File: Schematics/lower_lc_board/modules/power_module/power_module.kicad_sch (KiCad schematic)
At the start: 34 parts, among them J1 Stack Male Edge Connector, U1 TVS3300DRV, U10 ID_LM66100DCKR, U2 AMS1117, U3 ID_LM66100DCKR, U4 ID_LM66100DCKR

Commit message: routing work
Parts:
- added C50: 10uF, Capacitor_SMD:C_0603_1608Metric, symbol Device:C
- added C51: 1nF, Capacitor_SMD:C_0402_1005Metric, symbol Device:C
- added C52: 0.1uF, Capacitor_SMD:C_0402_1005Metric, symbol Device:C
- added TP13: 5V-TP, TestPoint:TestPoint_Pad_D1.0mm, symbol Connector:TestPoint
- C47: JLCPCB (none) -> C14663
- C7, C8: JLCPCB (none) -> C96446
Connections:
- net +3V3: now also C50.1, C51.1, C52.1
- net +5V: now also TP13.1
- net GND: now also C50.2, C51.2, C52.2

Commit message: routing work
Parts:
- R1: value 150 -> 220; footprint Resistor_SMD:R_0603_1608Metric -> Resistor_SMD:R_0402_1005Metric; JLCPCB (none) -> C25104
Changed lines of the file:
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@@
 			)
 		)
-		(property "Value" "150"
+		(property "Value" "220"
 			(at 66.04 102.87 90)
 			(effects
@@
 			)
 		)
-		(property "Footprint" "Resistor_SMD:R_0603_1608Metric"
+		(property "Footprint" "Resistor_SMD:R_0402_1005Metric"
 			(at 64.262 102.87 90)
 			(effects
@@
 			(at 66.04 102.87 0)
 			(effects
+				(font
+					(size 1.27 1.27)
+				)
+				(hide yes)
+			)
+		)
+		(property "JLCPCB" "C25104"
+			(at 66.04 102.87 0)
+			(effects

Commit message: routing work
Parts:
- removed C8: 10uF, Capacitor_SMD:C_0603_1608Metric, symbol Device:C
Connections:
- net 3V3_USB is gone; now on net GND: C6.1, TP6.1, U2.2 (VO), U4.1 (VIN)
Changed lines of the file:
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@@
 	)
 	(junction
-		(at 168.91 134.62)
-		(diameter 0)
-		(color 0 0 0 0)
-	)
-	(junction
 		(at 198.12 52.07)
 		(diameter 0)
@@
 	)
 	(junction
+		(at 168.91 134.62)
+		(diameter 0)
+		(color 0 0 0 0)
+	)
+	(junction
 		(at 208.28 62.23)
 		(diameter 0)
@@
 	(wire
 		(pts
+			(xy 168.91 134.62) (xy 190.5 134.62)
+		)
+		(stroke
+			(width 0)
+			(type default)
+		)
+	)
+	(wire
+		(pts
 			(xy 147.32 46.99) (xy 142.24 46.99)
 		)
@@
 	(wire
 		(pts
-			(xy 168.91 134.62) (xy 167.64 134.62)
+			(xy 167.64 134.62) (xy 168.91 134.62)
 		)
 		(stroke
@@
 	(wire
 		(pts
+			(xy 168.91 134.62) (xy 168.91 142.24)
+		)
+		(stroke
+			(width 0)
+			(type default)
+		)
+	)
+	(wire
+		(pts
 			(xy 87.63 133.35) (xy 87.63 134.62)
 		)
@@
 	(wire
 		(pts
-			(xy 168.91 134.62) (xy 190.5 134.62)
-		)
-		(stroke
-			(width 0)
-			(type default)
-		)
-	)
-	(wire
-		(pts
 			(xy 91.44 143.51) (xy 91.44 142.24)
 		)
@@
 		)
 	)
+	(label "3V3_USB"
+		(at 168.91 139.7 0)
+		(fields_autoplaced yes)
+		(effects
+			(font
+				(size 1.27 1.27)
+				(thickness 0.1588)
+			)
+			(justify left bottom)
+		)
+	)
 	(label "3V3_BP"
 		(at 106.68 38.1 180)
@@
 					(unit 1)
 				)
-			)
-		)
-	)
-	(symbol
-		(lib_id "Device:C")
-		(at 168.91 138.43 0)
-		(unit 1)
-		(exclude_from_sim no)
-		(in_bom yes)
-		(on_board yes)
-		(dnp no)
-		(property "Reference" "C8"
-			(at 171.45 137.16 0)
-			(effects
-				(font
-					(size 1.27 1.27)
-				)
-				(justify left)
-			)
-		)
-		(property "Value" "10uF"
-			(at 171.45 139.7 0)
-			(effects
-				(font
-					(size 1.27 1.27)
-				)
-				(justify left)
-			)
-		)
-		(property "Footprint" "Capacitor_SMD:C_0603_1608Metric"
-			(at 169.8752 142.24 0)
-			(effects
-				(font
-					(size 1.27 1.27)
-				)
-				(hide yes)
-			)
-		)
-		(property "Datasheet" "~"
-			(at 168.91 138.43 0)
-			(effects
-				(font
-					(size 1.27 1.27)
-				)
-				(hide yes)
-			)
-		)
-		(property "Description" ""
-			(at 168.91 138.43 0)
-			(effects
-				(font
-					(size 1.27 1.27)
-				)
-				(hide yes)
-			)
-		)
-		(property "LCSC" "C96446"
-			(at 168.91 138.43 0)
-			(effects
-				(font
-					(size 1.27 1.27)
-				)
-				(hide yes)
-			)
-		)
-		(property "JLCPCB" "C96446"
-			(at 168.91 138.43 0)
-			(effects
-				(font
-					(size 1.27 1.27)
-				)
-				(hide yes)
-			)
-		)
-		(pin "1"
-		)
-		(pin "2"
-		)
-		(instances
-			(project "lower_lc_board"
-				(path "/d63798c4-e363-437e-9012-e4aff32e6642/ea1dc739-d1f4-46a0-a090-2a1bf39da427"
-					(reference "C8")
-					(unit 1)
-				)

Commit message: more routing work
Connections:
- net GND: no longer C6.1, TP6.1, U2.2 (VO), U4.1 (VIN)
- new net 3V3_USB: C6.1, TP6.1, U2.2 (VO), U4.1 (VIN)
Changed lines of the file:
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@@
-	)
-	(junction
-		(at 168.91 134.62)
-		(diameter 0)
-		(color 0 0 0 0)
 	)
 	(junction
@@
 	(wire
 		(pts
-			(xy 168.91 134.62) (xy 190.5 134.62)
-		)
-		(stroke
-			(width 0)
-			(type default)
-		)
-	)
-	(wire
-		(pts
 			(xy 147.32 46.99) (xy 142.24 46.99)
 		)
@@
 	(wire
 		(pts
-			(xy 167.64 134.62) (xy 168.91 134.62)
+			(xy 167.64 134.62) (xy 190.5 134.62)
 		)
 		(stroke
@@
 	(wire
 		(pts
-			(xy 168.91 134.62) (xy 168.91 142.24)
-		)
-		(stroke
-			(width 0)
-			(type default)
-		)
-	)
-	(wire
-		(pts
 			(xy 87.63 133.35) (xy 87.63 134.62)
 		)
@@
 		(pts
 			(xy 87.63 134.62) (xy 86.36 134.62)
-		)
-		(stroke
-			(width 0)
-			(type default)
-		)
-	)
-	(wire
-		(pts
-			(xy 160.02 142.24) (xy 168.91 142.24)
 		)
 		(stroke
@@
 		(fields_autoplaced yes)
 		(effects
-			(font
-				(size 1.27 1.27)
-				(thickness 0.1588)
-			)
-			(justify left bottom)
-		)
-	)
-	(label "3V3_USB"
-		(at 168.91 139.7 0)
-		(fields_autoplaced yes)
-		(effects

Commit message: routing work
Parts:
- removed C1: 47uF, Capacitor_SMD:C_1206_3216Metric, symbol Device:C
- removed C47: 0.1uF, Capacitor_SMD:C_0603_1608Metric, symbol Device:C
- removed TP1: 24V_BP, TestPoint:TestPoint_Pad_D1.0mm, symbol Connector:TestPoint
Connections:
- net GND is gone; now on net +3V3: C2.2, C3.2, C4.2, C44.2, C5.1, C50.2, C51.2, C52.2, C6.2, C7.2, D1.1 (K), D2.1 (K), D3.1 (K), D4.1 (K), J1.A12 (GND_B), J1.A3 (GND_A), J1.A6 (GND_A), J1.A9 (GND_B), J1.B10 (GND_B), J1.B11 (GND_B), J1.B12 (GND_B), J1.B15 (GND_C), J1.B16 (GND_C), J1.B17 (GND_C), J1.B18 (GND_C), J1.B4 (GND_A), J1.B5 (GND_A), J1.B6 (GND_A), NT1.2, TP5.1, U1.1 (GND), U1.2 (GND), U1.3 (GND), U1.7 (GND), U10.2 (GND), U10.5 (ST), U2.1 (ADJ), U3.2 (GND), U3.5 (ST), U4.2 (GND), U4.5 (ST)
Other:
- moved on the sheet: TP2

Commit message: analog routing, start 3V3 power routing
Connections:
- net +3V3: no longer C2.2, C3.2, C4.2, C44.2, C5.1, C50.2, C51.2, C52.2, C6.2, C7.2, D1.1 (K), D2.1 (K), D3.1 (K), D4.1 (K), J1.A12 (GND_B), J1.A3 (GND_A), J1.A6 (GND_A), J1.A9 (GND_B), J1.B10 (GND_B), J1.B11 (GND_B), J1.B12 (GND_B), J1.B15 (GND_C), J1.B16 (GND_C), J1.B17 (GND_C), J1.B18 (GND_C), J1.B4 (GND_A), J1.B5 (GND_A), J1.B6 (GND_A), NT1.2, TP5.1, U1.1 (GND), U1.2 (GND), U1.3 (GND), U1.7 (GND), U10.2 (GND), U10.5 (ST), U2.1 (ADJ), U3.2 (GND), U3.5 (ST), U4.2 (GND), U4.5 (ST)
- new net GND: C2.2, C3.2, C4.2, C44.2, C5.1, C50.2, C51.2, C52.2, C6.2, C7.2, D1.1 (K), D2.1 (K), D3.1 (K), D4.1 (K), J1.A12 (GND_B), J1.A3 (GND_A), J1.A6 (GND_A), J1.A9 (GND_B), J1.B10 (GND_B), J1.B11 (GND_B), J1.B12 (GND_B), J1.B15 (GND_C), J1.B16 (GND_C), J1.B17 (GND_C), J1.B18 (GND_C), J1.B4 (GND_A), J1.B5 (GND_A), J1.B6 (GND_A), NT1.2, TP5.1, U1.1 (GND), U1.2 (GND), U1.3 (GND), U1.7 (GND), U10.2 (GND), U10.5 (ST), U2.1 (ADJ), U3.2 (GND), U3.5 (ST), U4.2 (GND), U4.5 (ST)
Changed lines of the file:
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@@
 	)
 	(junction
-		(at 60.96 114.3)
-		(diameter 0)
-		(color 0 0 0 0)
-	)
-	(junction
 		(at 142.24 46.99)
 		(diameter 0)
@@
 		(color 194 0 0 1)
 	)
-	(junction
-		(at 55.88 99.06)
-		(diameter 0)
-		(color 0 0 0 0)
-	)
 	(no_connect
 		(at 95.25 60.96)
@@
 	(wire
 		(pts
-			(xy 60.96 114.3) (xy 66.04 114.3)
-		)
-		(stroke
-			(width 0)
-			(type default)
-		)
-	)
-	(wire
-		(pts
 			(xy 96.52 93.98) (xy 100.33 93.98)
 		)
@@
 	(wire
 		(pts
-			(xy 55.88 99.06) (xy 55.88 114.3)
-		)
-		(stroke
-			(width 0)
-			(type default)
-		)
-	)
-	(wire
-		(pts
 			(xy 190.5 64.77) (xy 189.23 64.77)
 		)
@@
 	(wire
 		(pts
-			(xy 55.88 114.3) (xy 60.96 114.3)
-		)
-		(stroke
-			(width 0)
-			(type default)
-		)
-	)
-	(wire
-		(pts
 			(xy 198.12 62.23) (xy 198.12 72.39)
 		)
@@
 	(symbol
 		(lib_id "power:GND")
-		(at 60.96 114.3 0)
+		(at 66.04 114.3 0)
 		(unit 1)
 		(exclude_from_sim no)
@@
 		(dnp no)
 		(property "Reference" "#PWR03"
-			(at 60.96 120.65 0)
+			(at 66.04 120.65 0)
 			(effects
 				(font
@@
 		)
 		(property "Value" "GND"
-			(at 60.96 118.618 0)
+			(at 66.04 118.618 0)
 			(effects
 				(font
@@
 		)
 		(property "Footprint" ""
-			(at 60.96 114.3 0)
+			(at 66.04 114.3 0)
 			(effects
 				(font
@@
 		)
 		(property "Datasheet" ""
-			(at 60.96 114.3 0)
+			(at 66.04 114.3 0)
 			(effects
 				(font
@@
 		)
 		(property "Description" "Power symbol creates a global label with name \"GND\" , ground"
-			(at 60.96 114.3 0)
+			(at 66.04 114.3 0)
 			(effects
 				(font

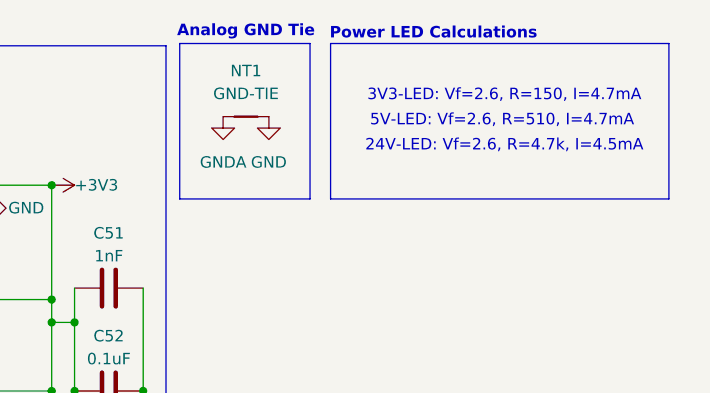
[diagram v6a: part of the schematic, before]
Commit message: remove AGND
simplicity
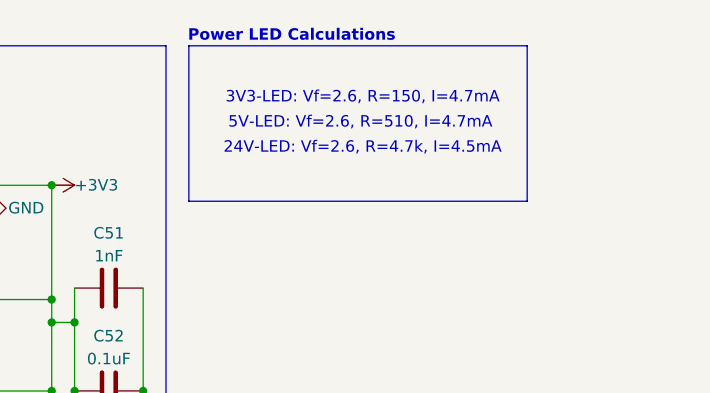
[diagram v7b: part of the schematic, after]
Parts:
- removed NT1: GND-TIE, NetTie:NetTie-2_SMD_Pad0.5mm, symbol Device:NetTie_2
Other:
- note removed: "Analog GND Tie"
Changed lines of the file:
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@@
 	)
 	(rectangle
-		(start 229.108 23.622)
-		(end 266.7 40.894)
+		(start 213.36 23.876)
+		(end 250.952 41.148)
 		(stroke
 			(width 0)
@@
 	)
 	(rectangle
-		(start 212.344 23.622)
-		(end 226.822 40.894)
-		(stroke
-			(width 0)
-			(type default)
-			(color 0 0 0 1)
-		)
-		(fill
-			(type none)
-		)
-	)
-	(rectangle
 		(start 130.302 23.876)
 		(end 210.82 101.6)
@@
 	(text "24V-LED: Vf=2.6, R=4.7k, I=4.5mA"
 		(exclude_from_sim no)
-		(at 248.412 35.052 0)
+		(at 232.664 35.306 0)
 		(effects
 			(font
@@
 	(text "3V3-LED: Vf=2.6, R=150, I=4.7mA"
 		(exclude_from_sim no)
-		(at 248.412 29.464 0)
+		(at 232.664 29.718 0)
 		(effects
 			(font
@@
 		)
 	)
-	(text "Analog GND Tie"
-		(exclude_from_sim no)
-		(at 219.71 22.352 0)
-		(effects
-			(font
-				(size 1.27 1.27)
-				(thickness 0.254)
-				(bold yes)
-				(color 0 0 0 1)
-			)
-		)
-	)
 	(text "Power LED Calculations\n"
 		(exclude_from_sim no)
-		(at 240.538 22.606 0)
+		(at 224.79 22.86 0)
 		(effects
 			(font
@@
 	(text "5V-LED: Vf=2.6, R=510, I=4.7mA"
 		(exclude_from_sim no)
-		(at 248.158 32.258 0)
+		(at 232.41 32.512 0)
 		(effects
 			(font
@@
 	)
 	(symbol
-		(lib_id "power:GND")
-		(at 222.25 31.75 0)
-		(unit 1)
-		(exclude_from_sim no)
-		(in_bom yes)
-		(on_board yes)
-		(dnp no)
-		(fields_autoplaced yes)
-		(property "Reference" "#PWR0108"
-			(at 222.25 38.1 0)
-			(effects
-				(font
-					(size 1.27 1.27)
-				)
-				(hide yes)
-			)
-		)
-		(property "Value" "GND"
-			(at 222.25 36.83 0)
-			(effects
-				(font
-					(size 1.27 1.27)
-				)
-			)
-		)
-		(property "Footprint" ""
-			(at 222.25 31.75 0)
-			(effects
-				(font
-					(size 1.27 1.27)
-				)
-				(hide yes)
-			)
-		)
-		(property "Datasheet" ""
-			(at 222.25 31.75 0)
-			(effects
-				(font
-					(size 1.27 1.27)
-				)
-				(hide yes)
-			)
-		)
-		(property "Description" "Power symbol creates a global label with name \"GND\" , ground"
-			(at 222.25 31.75 0)
-			(effects
-				(font
-					(size 1.27 1.27)
-				)
-				(hide yes)
-			)
-		)
-		(pin "1"
-		)
-		(instances
-			(project ""
-				(path "/d63798c4-e363-437e-9012-e4aff32e6642/ea1dc739-d1f4-46a0-a090-2a1bf39da427"
-					(reference "#PWR0108")
-					(unit 1)
-				)
-			)
-		)
-	)
-	(symbol
 		(lib_id "Device:LED")
 		(at 104.14 105.41 90)
@@
 	)
 	(symbol
-		(lib_id "power:GNDA")
-		(at 217.17 31.75 0)
-		(unit 1)
-		(exclude_from_sim no)
-		(in_bom yes)
-		(on_board yes)
-		(dnp no)
-		(fields_autoplaced yes)
-		(property "Reference" "#PWR0109"
-			(at 217.17 38.1 0)
-			(effects
-				(font
-					(size 1.27 1.27)
-				)
-				(hide yes)
-			)
-		)
-		(property "Value" "GNDA"
-			(at 217.17 36.83 0)
-			(effects
-				(font
-					(size 1.27 1.27)
-				)
-			)
-		)
-		(property "Footprint" ""
-			(at 217.17 31.75 0)
-			(effects
-				(font
-					(size 1.27 1.27)
-				)
-				(hide yes)
-			)
-		)
-		(property "Datasheet" ""
-			(at 217.17 31.75 0)
-			(effects
-				(font
-					(size 1.27 1.27)
-				)
-				(hide yes)
-			)
-		)
-		(property "Description" "Power symbol creates a global label with name \"GNDA\" , analog ground"
-			(at 217.17 31.75 0)
-			(effects
-				(font
-					(size 1.27 1.27)
-				)
-				(hide yes)
-			)
-		)
-		(pin "1"
-		)
-		(instances
-			(project ""
-				(path "/d63798c4-e363-437e-9012-e4aff32e6642/ea1dc739-d1f4-46a0-a090-2a1bf39da427"
-					(reference "#PWR0109")
-					(unit 1)
-				)
-			)
-		)
-	)
-	(symbol
 		(lib_id "power:GND")
 		(at 143.51 69.85 0)
@@
 					(unit 1)
 				)
-			)
-		)
-	)
-	(symbol
-		(lib_id "Device:NetTie_2")
-		(at 219.71 31.75 0)
-		(unit 1)
-		(exclude_from_sim no)
-		(in_bom no)
-		(on_board yes)
-		(dnp no)
-		(fields_autoplaced yes)
-		(property "Reference" "NT1"
-			(at 219.71 26.67 0)
-			(effects
-				(font
-					(size 1.27 1.27)
-				)
-			)
-		)
-		(property "Value" "GND-TIE"
-			(at 219.71 29.21 0)
-			(effects
-				(font
-					(size 1.27 1.27)
-				)
-			)
-		)
-		(property "Footprint" "NetTie:NetTie-2_SMD_Pad0.5mm"
-			(at 219.71 31.75 0)
-			(effects
-				(font
-					(size 1.27 1.27)
-				)
-				(hide yes)
-			)
-		)
-		(property "Datasheet" "~"
-			(at 219.71 31.75 0)
-			(effects
-				(font
-					(size 1.27 1.27)
-				)
-				(hide yes)
-			)
-		)
-		(property "Description" "Net tie, 2 pins"
-			(at 219.71 31.75 0)
-			(effects
-				(font
-					(size 1.27 1.27)
-				)
-				(hide yes)
-			)
-		)
-		(pin "1"
-		)
-		(pin "2"
-		)
-		(instances
-			(project ""
-				(path "/d63798c4-e363-437e-9012-e4aff32e6642/ea1dc739-d1f4-46a0-a090-2a1bf39da427"
-					(reference "NT1")
-					(unit 1)
-				)

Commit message: adjust routing for 0603 min. footprints
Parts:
- R1: footprint Resistor_SMD:R_0402_1005Metric -> Resistor_SMD:R_0603_1608Metric; JLCPCB C25104 -> (none)
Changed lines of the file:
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@@
 			)
 		)
-		(property "Footprint" "Resistor_SMD:R_0402_1005Metric"
+		(property "Footprint" "Resistor_SMD:R_0603_1608Metric"
 			(at 64.262 102.87 90)
 			(effects
@@
 			)
 		)
-		(property "JLCPCB" "C25104"
+		(property "JLCPCB" ""
 			(at 66.04 102.87 0)
 			(effects
